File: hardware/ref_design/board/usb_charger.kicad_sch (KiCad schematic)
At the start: 20 parts, among them J1 TYPE-C-31-M-12, J2 S2B-PH-SM4-TB, Q2 AO3401A, U1 SRV05-4, U2 TP4056-42-ESOP8

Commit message: Reference design: audit round 3 fixes (unplug hand-over, panel stack)
- R38 (VBUS bleeder) 10k -> 1k. At an unplug C1 held VBUS up, and Q2's gate,
  fed from VBUS through D6, could only fall as fast as VBUS: the body diode
  carried the system for tens of ms at the cell less 0.5 V. Now Q2 conducts
  about 3 ms after an unplug, fully on after about 8 ms. 5 mA on USB. The
  design review's "microseconds" description of the hand-over was wrong and
  is rewritten; the bring-up unplug test says what to expect.
- Panel counted as 2.45 mm (the drawing's side view says 2.35 +-0.1) and the
  0.15 mm tape is in the stack: the glass limit drops to 2.1 mm (J3's 2.0 mm
  still clears). Window margin 1.0 mm (float, tolerance and print error).
  The lid's FPC notch widened: the drawing doesn't dimension the neck, so
  fpc_neck is marked ESTIMATE.

Checks: netlist PASS (123 parts), ERC 0, DRC 0 errors / 0 unconnected /
0 parity (2 cosmetic silk warnings), fit PASS on 92 parts.

Co-Authored-By: Claude Opus 5.5 <noreply@anthropic.com>
Claude-Session: https://claude.ai/code/session_01KGgEu3CbFtCsvHRQgAFiCN
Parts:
- R38: value 10k -> 1k; LCSC C25744 -> C11702; MPN 0402WGF1002TCE -> 0402WGF1001TCE
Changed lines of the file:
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@@
         (font
           (size 1.27 1.27))))
-    (property "Value" "10k"
+    (property "Value" "1k"
       (at 109.22 77.47 0)
       (effects
@@
           (size 1.27 1.27))
         (hide yes)))
-    (property "LCSC" "C25744"
+    (property "LCSC" "C11702"
       (at 0 0 0)
       (effects
@@
           (size 1.27 1.27))
         (hide yes)))
-    (property "MPN" "0402WGF1002TCE"
+    (property "MPN" "0402WGF1001TCE"
       (at 0 0 0)
       (effects

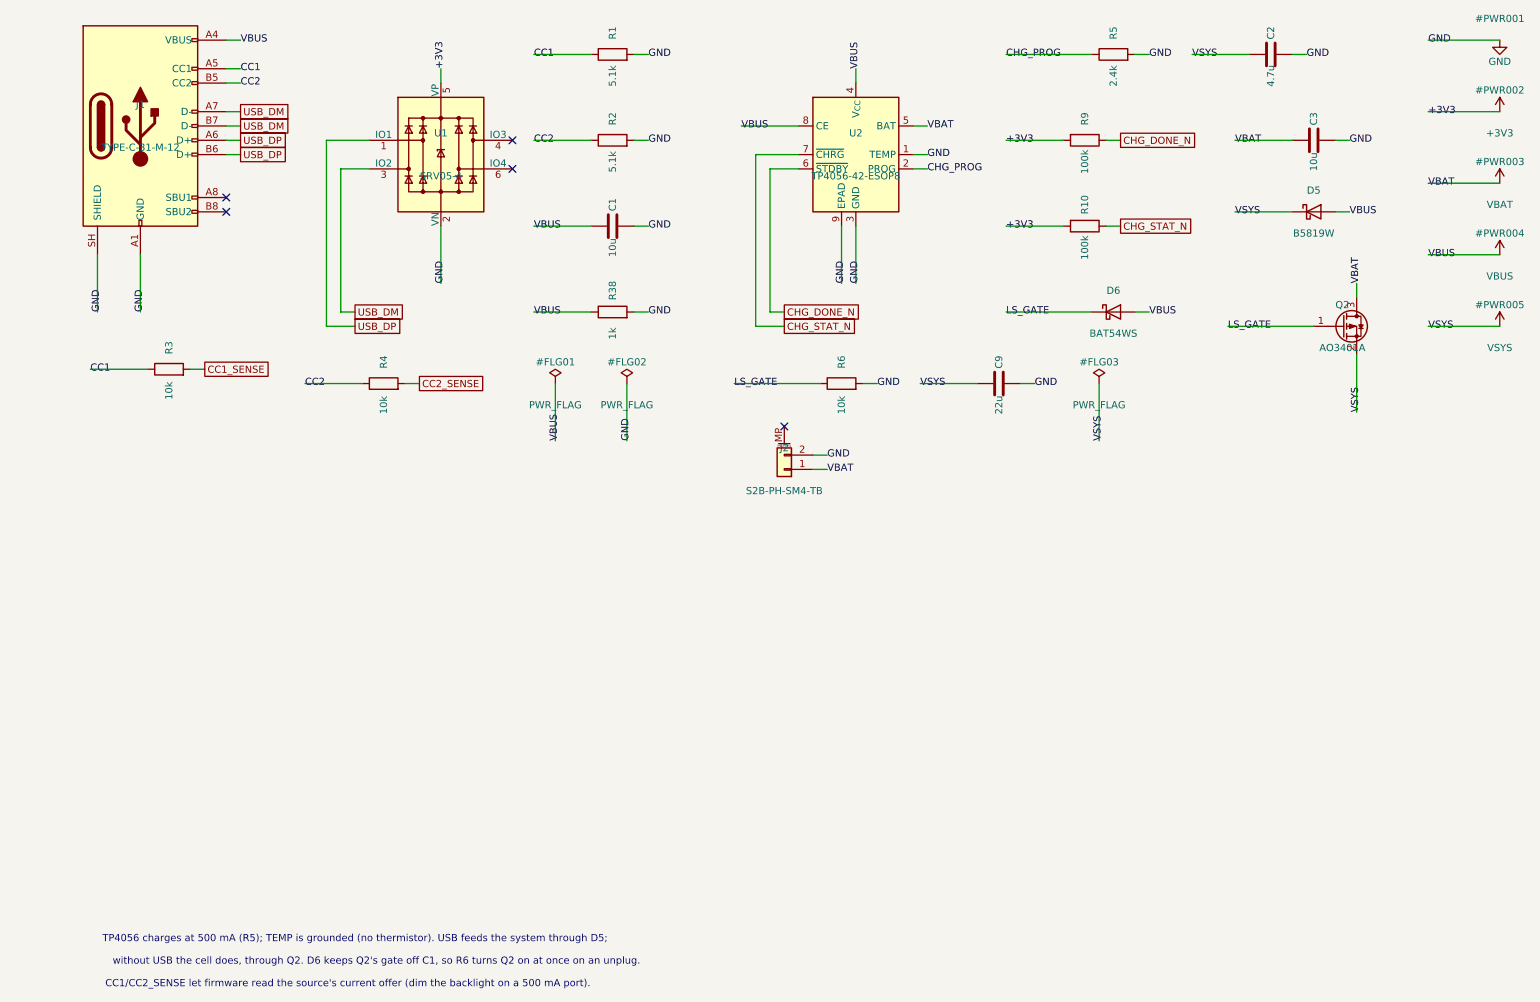
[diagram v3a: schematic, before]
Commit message: Reference design: charge thermistor, genuine DS Lite caps on stepped decks, keyed pin
- TH1 (NCP15XH103F03RC) on the TP4056's TEMP with R39 5.6k / R40 150k from VBUS:
  charges from 1 to 46 C; sits over the cell's edge, 45 mm from U2
- Caps measured from open models of genuine DS Lite parts (case/DSLITE.md): 7.0 mm
  ABXY with an 8.8 mm flange; flange pockets with a 30 degree slot for each cap's tab
- The lid face over the screen left the caps 0.84 mm under it, so each end steps down
  2.14 mm to a button deck (a spine stays up over J2 and the end hooks): caps 1.3 proud
- Seat 1's centre locating pin 3 mm off centre: board and lid fit one way only
- route.py: click Freerouting's warning dialog's OK where it is (bottom right); the
  missed click left runs hanging

Co-Authored-By: Claude Opus 5.5 <noreply@anthropic.com>
Claude-Session: https://claude.ai/code/session_01KGgEu3CbFtCsvHRQgAFiCN
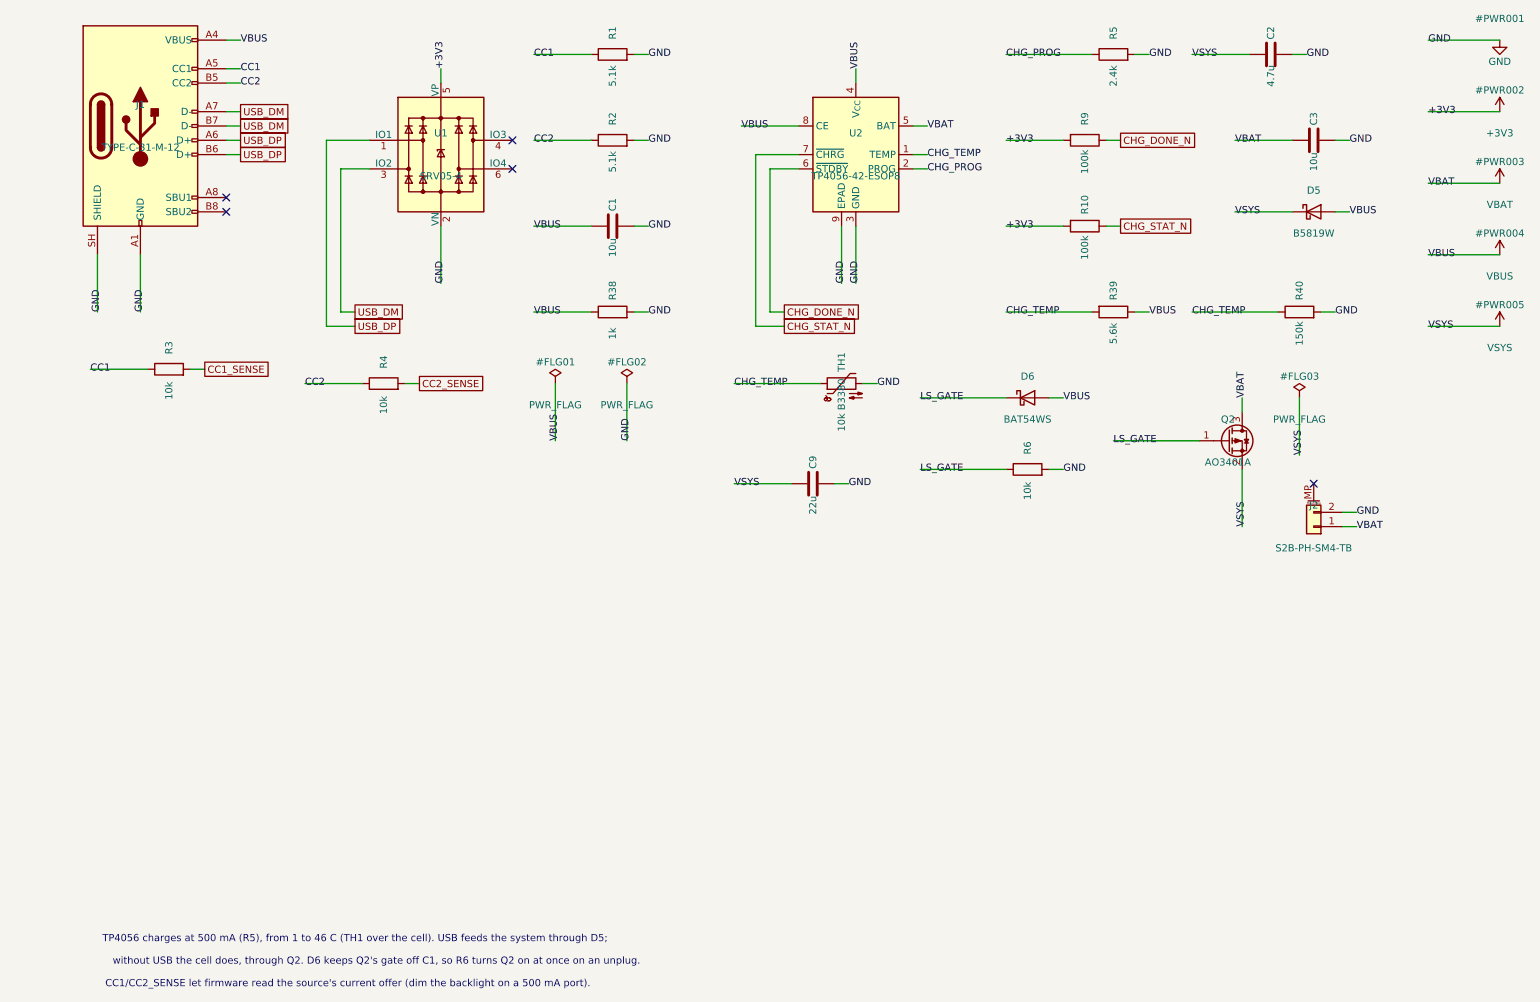
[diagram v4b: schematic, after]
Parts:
- added R39: 5.6k, Resistor_SMD:R_0402_1005Metric, symbol Device:R
- added R40: 150k, Resistor_SMD:R_0402_1005Metric, symbol Device:R
- added TH1: 10k B3380, Resistor_SMD:R_0402_1005Metric, symbol Device:Thermistor_NTC
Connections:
- net GND: now also R40.2, TH1.2; no longer U2.1 (TEMP)
- net VBUS: now also R39.1
- new net CHG_TEMP: R39.2, R40.1, TH1.1, U2.1 (TEMP)
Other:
- note added: "TP4056 charges at 500 mA (R5), from 1 to 46 C (TH1 over the cell). USB feeds the system through D5;"
- note removed: "TP4056 charges at 500 mA (R5); TEMP is grounded (no thermistor). USB feeds the system through D5;"

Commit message: Reference design: settle the open decisions (Fable/Opus debate)
Two independent model reviews, two rounds each, converged on:
- D7, a B5819W across Q2, fitted: as built, 3V3 fell under the internal
  flash's 2.97 V minimum on every unplug with the cell below about 3.7 V
  (Q2's body diode drops 0.6 V at 0.25 A); with D7 it holds down to
  about 3.42 V, inside the 3.5 V cutoff
- R38 to an 0603 (C21190): 25-30% loaded instead of 44-48%, free in the
  re-route D7 forced
- R41, 2.2 ohm in series with C1: the TP4056 datasheet's fix for a ceramic
  input cap ringing at hot plug (no cell, 2 m cable: VSYS 6.7 -> 6.2 V
  against the ME6211's 6.5 V maximum). No TVS: an SMF5.0A is rated below
  USB's 5.5 V and would barely conduct
- Kept: the 470k/470k divider (off-state drain, the unpowered pad) and every
  copper width (no trace carries more than about 0.5 A)
- Firmware: the ADC reads against 3V3, which follows the cell once the LDO
  drops out, so the computed VBAT levels off at 3.37-3.43 V: cut off at
  3.5 V, calibrate at charge-done, keep the ADC channel alive
Bring-up gains a no-cell hot-plug scope check.

Co-Authored-By: Claude Opus 5.5 <noreply@anthropic.com>
Claude-Session: https://claude.ai/code/session_01KGgEu3CbFtCsvHRQgAFiCN
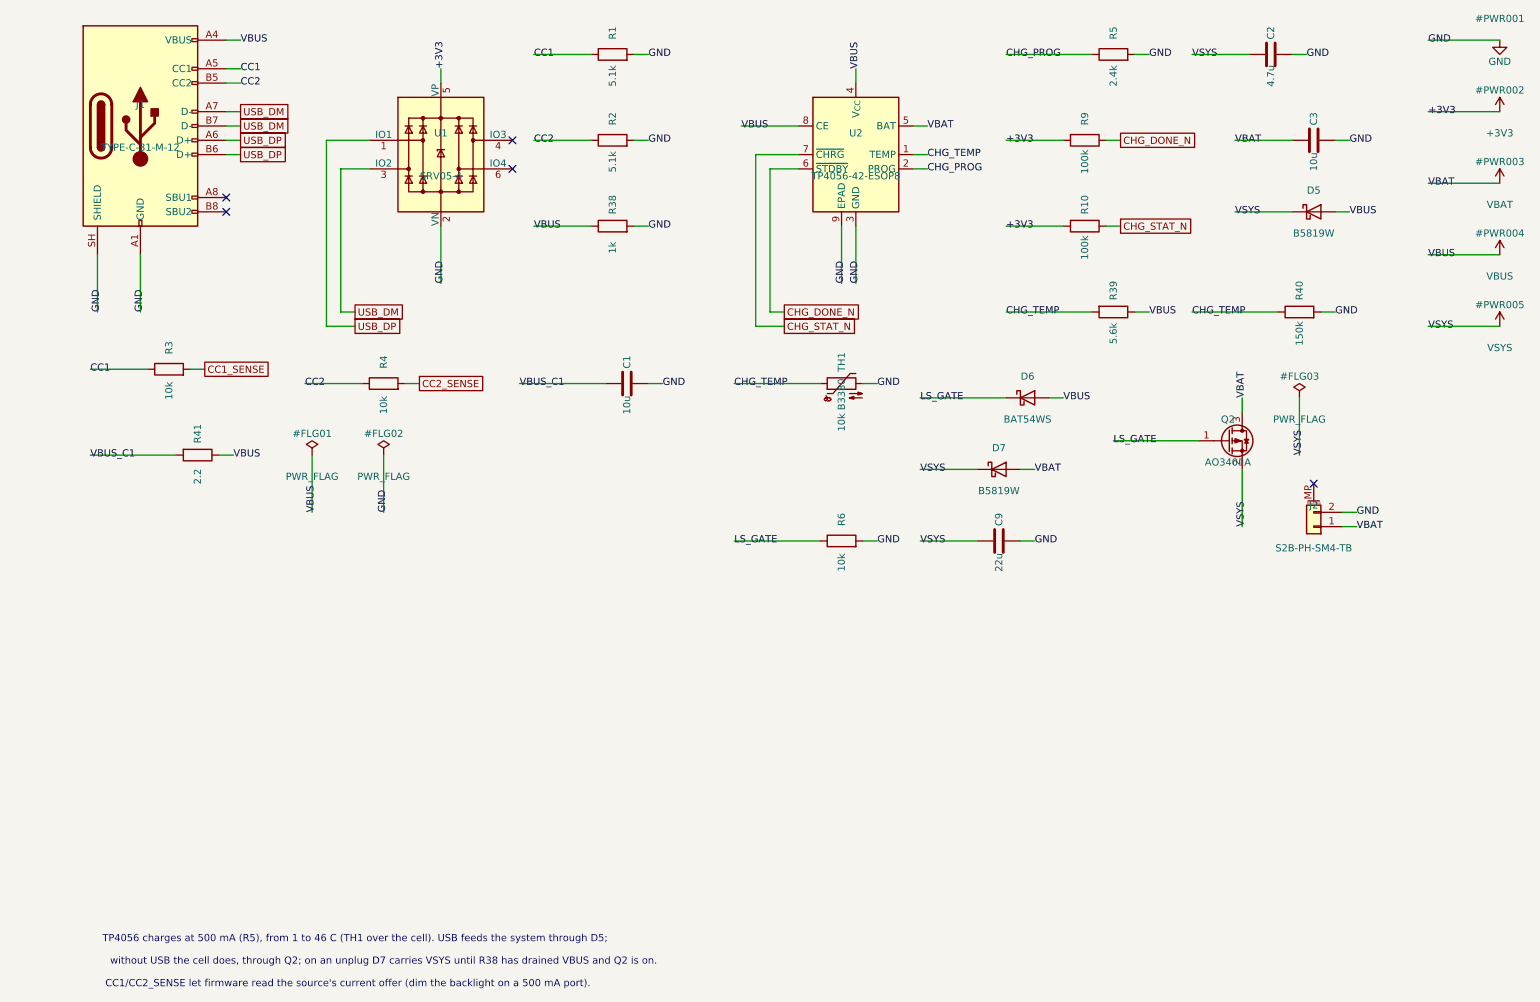
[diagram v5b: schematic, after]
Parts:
- added D7: B5819W, Diode_SMD:D_SOD-123, symbol Device:D_Schottky
- added R41: 2.2, Resistor_SMD:R_0603_1608Metric, symbol Device:R
- R38: footprint Resistor_SMD:R_0402_1005Metric -> Resistor_SMD:R_0603_1608Metric; LCSC C11702 -> C21190; MPN 0402WGF1001TCE -> 0603WAF1001T5E
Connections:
- net VBAT: now also D7.2 (A)
- net VBUS: now also R41.1; no longer C1.1
- net VSYS: now also D7.1 (K)
- new net VBUS_C1: C1.1, R41.2
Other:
- note added: "without USB the cell does, through Q2; on an unplug D7 carries VSYS until R38 has drained VBUS and Q2 is on."
- note removed: "without USB the cell does, through Q2. D6 keeps Q2's gate off C1, so R6 turns Q2 on at once on an unplug."

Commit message: Reference design: checklist changes and the datasheet pin gate
Board: PWR_HOLD pull-down (R42, also covers RP2350-E9), charge current
3.3k (333-364 mA), firmware charge pause (CHG_OFF, Q4), R13 33k, 0.1 ohm
in D5's path, JP1/JP2 cut-jumpers, TP6-8, spare 1206 footprints, 4-bit
revision strap on GPIO22-25 (REV 1 on the back).

Datasheet review of every part's pins (pin_review/, tools/check_pins.py)
found and fixed: J6 TX/RX swapped against Raspberry Pi's debug connector
spec, USB series resistors 22 to 27 ohm, the ME6211 CE able to lead its
VIN at a live plug-in (C47 on PWR_EN).

Case: silicone height 1.2 mm from the DS Lite, chamfered step.

Co-Authored-By: Claude Opus 5.5 <noreply@anthropic.com>
Claude-Session: https://claude.ai/code/session_01MUt6paNsT75sqwAr83zRS3
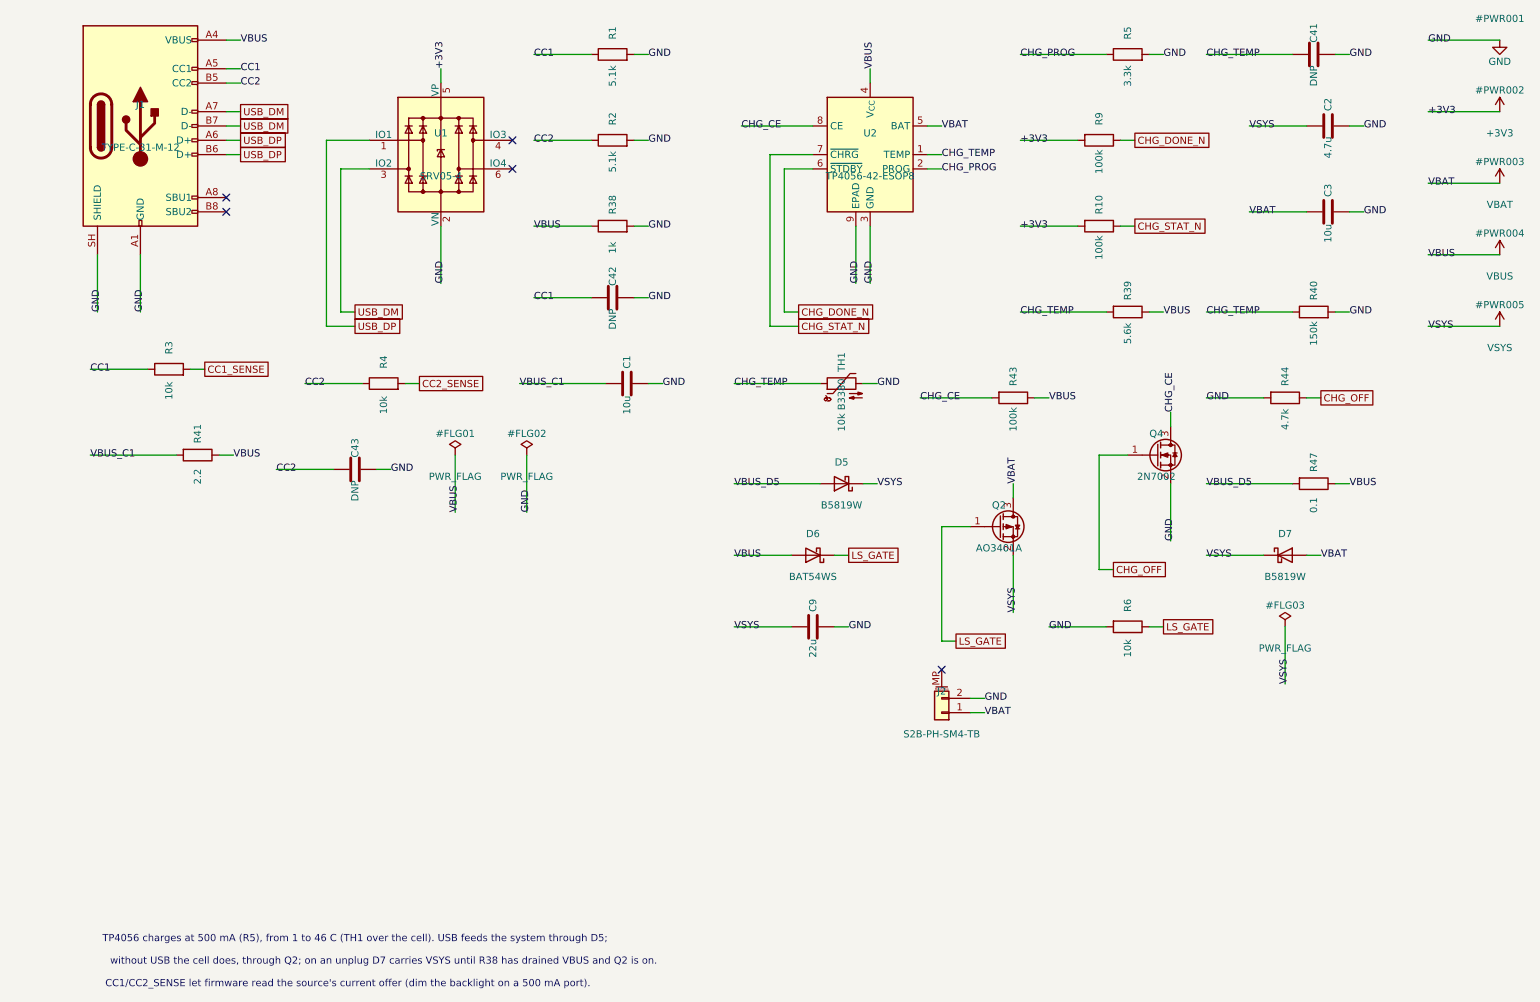
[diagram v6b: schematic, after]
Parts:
- added C41, C42, C43: DNP, Capacitor_SMD:C_1206_3216Metric, symbol Device:C
- added Q4: 2N7002, Package_TO_SOT_SMD:SOT-23, symbol Transistor_FET:Q_NMOS_GSD
- added R43: 100k, Resistor_SMD:R_0402_1005Metric, symbol Device:R
- added R44: 4.7k, Resistor_SMD:R_0402_1005Metric, symbol Device:R
- added R47: 0.1, Resistor_SMD:R_1206_3216Metric, symbol Device:R
- R5: value 2.4k -> 3.3k; LCSC C25882 -> C25890; MPN 0402WGF2401TCE -> 0402WGF3301TCE
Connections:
- net CC1: now also C42.1
- net CC2: now also C43.1
- net CHG_TEMP: now also C41.1
- net GND: now also C41.2, C42.2, C43.2, Q4.2 (S), R44.2
- net VBUS: now also R43.1, R47.1; no longer D5.2 (A), U2.8 (CE)
- new net CHG_CE: Q4.3 (D), R43.2, U2.8 (CE)
- new net CHG_OFF: Q4.1 (G), R44.1
- new net VBUS_D5: D5.2 (A), R47.2

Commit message: Reference design: U1 to Semtech SRV05-4.TCT (C13612), ProTek C85364 out of stock
JLC had 2 of ProTek's SRV05-4-P-T7 left. Semtech's SRV05-4.TCT has the same
pinout (1, 3, 4, 6 I/O; 2 ground; 5 positive reference, datasheet p1, p2, p5),
the same SOT-23-6 outline and the same JLC library footprint, so the CPL
rotation is unchanged. 3 pF typ / 5 pF max, 5 uA, +-8 kV contact.

It is plain Extended (C85364 was Preferred): one more $3.07 feeder fee,
13 extended part numbers; docs/bom.md and PLAN.md updated. pin_review/u1.json
now cites the Semtech datasheet (Revision 08/11/04, LCSC copy).

Schematic regenerated with build_sch.py; the board's footprints relinked to
the new symbol UUIDs and U1's fields set with pcbnew (no placement or copper
change). check_netlist, check_pins, ERC and check_pcb pass; fab outputs
regenerated (BOM line changes; gerbers differ only in timestamps).

Co-Authored-By: Claude Opus 5.5 <noreply@anthropic.com>
Claude-Session: https://claude.ai/code/session_01Ceq1EsbekLwXHokcQ73Ldk
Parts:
- U1: LCSC C85364 -> C13612; MPN SRV05-4-P-T7 -> SRV05-4.TCT; Manufacturer ProTek Devices -> Semtech
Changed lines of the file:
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@@
           (size 1.27 1.27))
         (hide yes)))
-    (property "LCSC" "C85364"
+    (property "LCSC" "C13612"
       (at 0 0 0)
       (effects
@@
           (size 1.27 1.27))
         (hide yes)))
-    (property "MPN" "SRV05-4-P-T7"
+    (property "MPN" "SRV05-4.TCT"
       (at 0 0 0)
       (effects
@@
           (size 1.27 1.27))
         (hide yes)))
-    (property "Manufacturer" "ProTek Devices"
+    (property "Manufacturer" "Semtech"
       (at 0 0 0)
       (effects
